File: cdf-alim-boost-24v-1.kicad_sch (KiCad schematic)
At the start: 53 parts, among them J1 Conn_01x02, J2 Conn_01x02, Q3 BSC019N04LS, Q4 BSC019N04LS, Q5 BSC019N04LS, Q6 BSC019N04LS, U2 LM5122

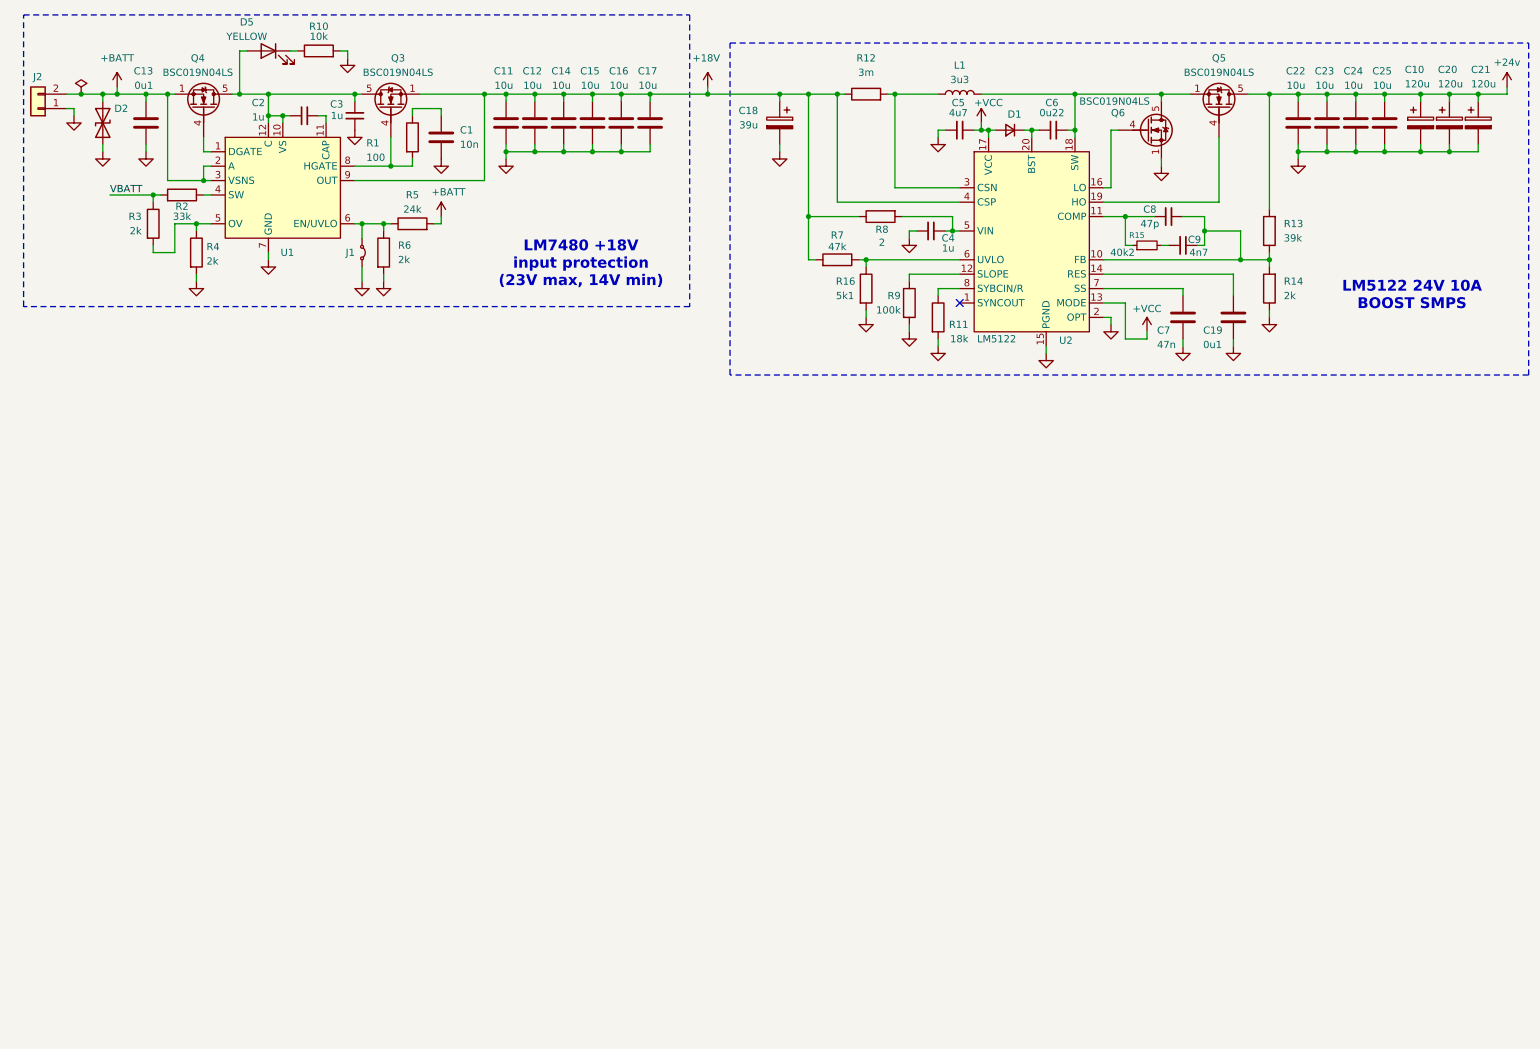
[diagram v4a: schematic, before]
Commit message: schem: add TPS25983 10A 24V output efuse
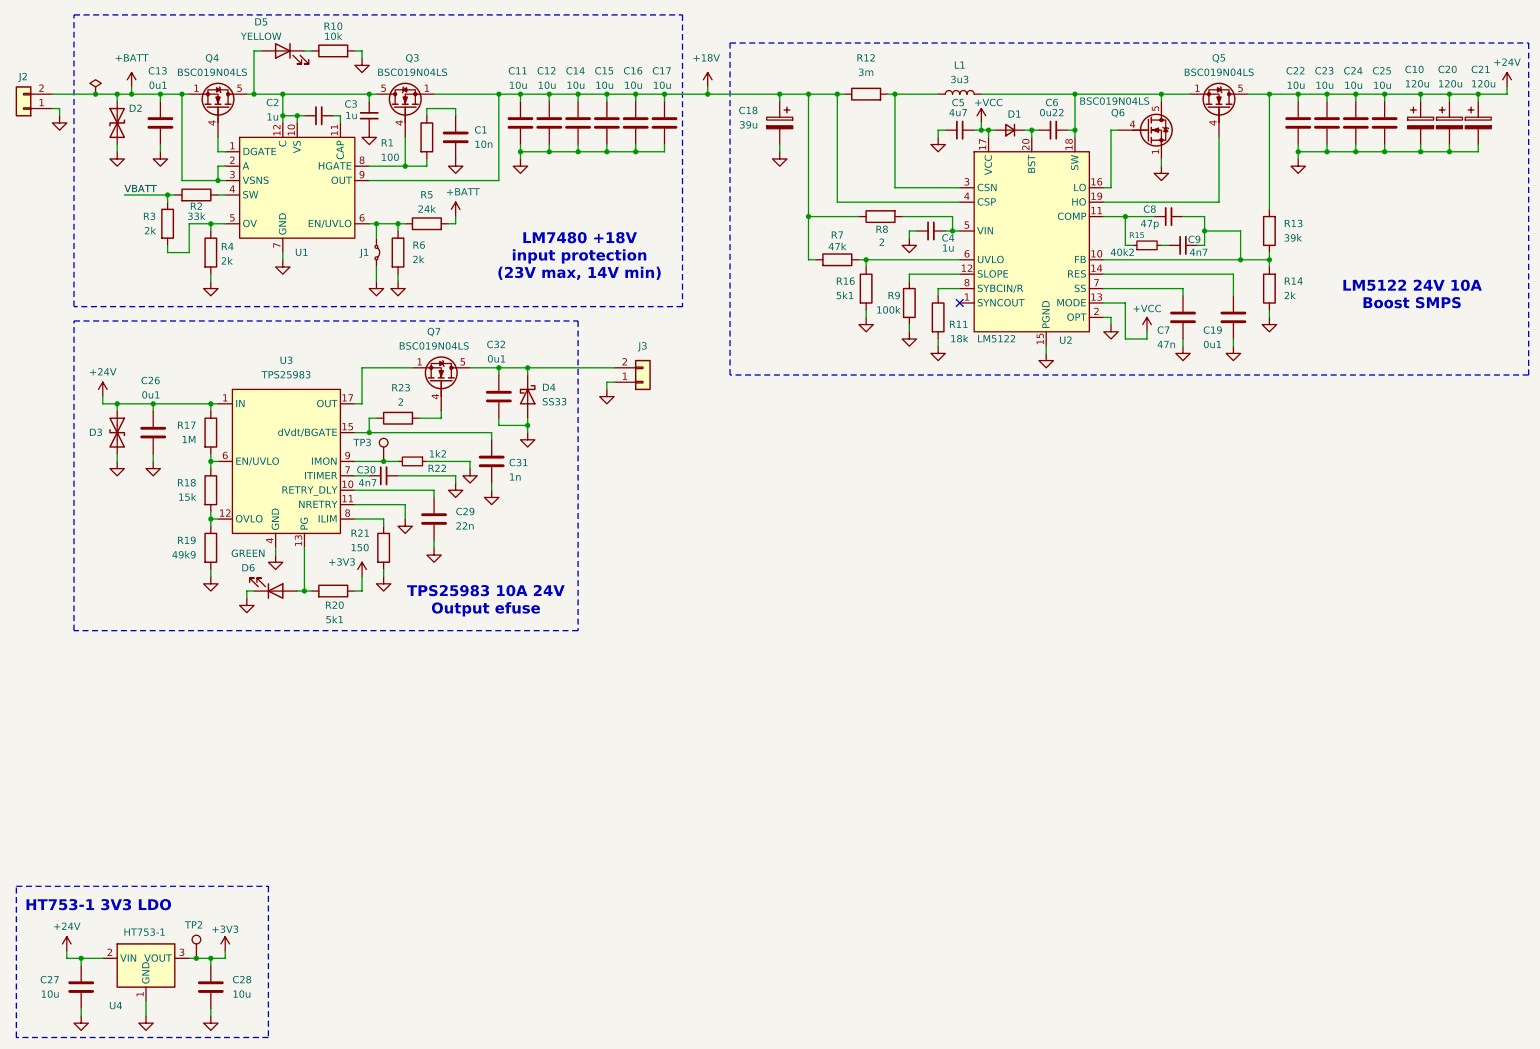
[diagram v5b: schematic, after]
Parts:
- added C26, C32: 0u1, Capacitor_SMD:C_0402_1005Metric, symbol Device:C
- added C27, C28: 10u, Capacitor_SMD:C_0805_2012Metric, symbol Device:C
- added C29: 22n, symbol Device:C
- added C30: 4n7, symbol Device:C_Small
- added C31: 1n, symbol Device:C
- added D3: SMAJ26CA, Diode_SMD:D_SMA, symbol Device:D_TVS
- added D4: SS33, GLCS:Texas_RGE0024M_VQFN-24-1EP_4x4mm_P0.5mm_ThermalVias, symbol Device:D_Schottky
- added D6: GREEN, LED_SMD:LED_0805_2012Metric, symbol Device:LED
- added J3: Conn_01x02, symbol Connector_Generic:Conn_01x02
- added Q7: BSC019N04LS, Package_TO_SOT_SMD:TDSON-8-1, symbol Transistor_FET:CSD18501Q5A
- added R17: 1M, symbol Device:R
- added R18: 15k, symbol Device:R
- added R19: 49k9, symbol Device:R
- added R20: 5k1, Resistor_SMD:R_0402_1005Metric, symbol Device:R
- added R21: 150, symbol Device:R
- added R22: 1k2, symbol Device:R_Small
- added R23: 2, symbol Device:R
- added TP2, TP3: TestPoint, TestPoint:TestPoint_Pad_D2.0mm, symbol Connector:TestPoint
- added U3: TPS25983, GLCS:Texas_RGE0024M_VQFN-24-1EP_4x4mm_P0.5mm_ThermalVias, symbol GLCS:TPS25983
- added U4: HT753-1, Package_TO_SOT_SMD:SOT-89-3, symbol Regulator_Linear:HT75xx-1-SOT89
- J2: footprint Connector_JST:JST_XH_S2B-XH-A-1_1x02_P2.50mm_Horizontal -> (none)
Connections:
- net AGND: now also C26.2, C27.2, C28.2, C29.2, C30.2, C31.1, C32.2, D3.2 (A2), D4.2 (A), D6.1 (K), J3.1 (Pin_1), R19.2, R21.2, R22.1, U3.11 (NRETRY), U3.14 (GND), U3.26 (GND), U3.4 (GND), U3.5 (GND), U4.1 (GND)
- net +24v renamed +24V
- net +24V: now also C26.1, C27.1, D3.1 (A1), R17.1, U3.1 (IN), U3.16 (IN), U3.2 (IN), U3.25 (IN), U3.3 (IN), U4.2 (VIN)
- new net: C30.1, U3.7 (ITIMER)
- new net: D6.2 (A), R20.2, U3.13 (PG)
- new net: R18.2, R19.1, U3.12 (OVLO)
- new net: C31.2, R23.1, U3.15 (dVdt/BGATE)
- new net: Q7.4 (G), R23.2
- new net: R21.1, U3.8 (ILIM)
- new net: R17.2, R18.1, U3.6 (EN/UVLO)
- new net: R22.2, TP3.1, U3.9 (IMON)
- new net: C32.1, D4.1 (K), J3.2 (Pin_2), Q7.5 (D)
- new net: C29.1, U3.10 (RETRY_DLY)
- new net: Q7.1 (S), Q7.2 (S), Q7.3 (S), U3.17 (OUT), U3.18 (OUT), U3.19 (OUT), U3.20 (OUT), U3.21 (OUT), U3.22 (OUT), U3.23 (OUT), U3.24 (OUT)
- new net +3V3: C28.1, R20.1, TP2.1, U4.3 (VOUT)
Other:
- note added: "HT753-1 3V3 LDO"
- note added: "LM5122 24V 10A Boost SMPS"
- note added: "TPS25983 10A 24V Output efuse"
- note removed: "LM5122 24V 10A BOOST SMPS"
- moved on the sheet: C1, C11, C12, C13, C14, C15, C16, C17, C2, C3, D2, D5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

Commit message: schem: add test points
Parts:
- added TP10, TP11, TP12, TP13, TP14, TP4, TP5, TP6, TP7, TP8, TP9: TestPoint, TestPoint:TestPoint_Pad_D2.0mm, symbol Connector:TestPoint
- added TP15: TestPoint, TestPoint:TestPoint_Pad_D2.0mm, symbol Connector:TestPoint_Small
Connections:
- net +18V: now also TP5.1, TP7.1
- net +24V: now also TP10.1, TP11.1
- net +BATT: now also TP6.1
- net at R3.2, R4.1, U1.5 (OV): now also TP14.1
- net at C6.1, L1.2, Q5.1 (S)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: now also TP9.1
- net at L1.1, R12.2, U2.3 (CSN): now also TP8.1
- net at R21.1, U3.8 (ILIM): now also TP15.1
- net at C32.1, D4.1 (K), J3.2 (Pin_2)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: now also TP13.1
- net at C2.2, C3.2, D5.2 (A)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: now also TP4.1
- net at Q7.1 (S), Q7.2 (S), Q7.3 (S)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: now also TP12.1

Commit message: schem: run and fix ERC
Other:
- moved on the sheet: C4

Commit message: schem: add footprints
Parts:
- J2: footprint (none) -> Connector_AMASS:AMASS_XT30PW-M_1x02_P2.50mm_Horizontal
- J3: footprint (none) -> Connector_AMASS:AMASS_XT30PW-F_1x02_P2.50mm_Horizontal
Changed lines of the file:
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@@
 			)
 		)
-		(property "Footprint" ""
+		(property "Footprint" "Connector_AMASS:AMASS_XT30PW-F_1x02_P2.50mm_Horizontal"
 			(at 124.46 80.01 0)
 			(hide yes)
@@
 			)
 		)
-		(property "Footprint" ""
+		(property "Footprint" "Connector_AMASS:AMASS_XT30PW-M_1x02_P2.50mm_Horizontal"
 			(at 15.24 31.75 0)
 			(hide yes)
